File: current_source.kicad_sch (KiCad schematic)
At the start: 7 parts, among them J4 From_E-stop, Q3 S8050, Q4 BSS84, U3 LM317L

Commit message: Termianl block 3d view
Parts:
- J4: value From_E-stop -> TB0010-500-02GR; footprint TerminalBlock:TerminalBlock_MaiXu_MX126-5.0-02P_1x02_P5.00mm -> lighthouse:TerminalBlock_TB0010-500-02GR_1x02_P5.00mm
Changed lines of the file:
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@@
 			)
 		)
-		(property "Value" "From_E-stop"
+		(property "Value" "TB0010-500-02GR"
 			(at 167.64 62.23 0)
 			(effects
@@
 			)
 		)
-		(property "Footprint" "TerminalBlock:TerminalBlock_MaiXu_MX126-5.0-02P_1x02_P5.00mm"
+		(property "Footprint" "lighthouse:TerminalBlock_TB0010-500-02GR_1x02_P5.00mm"
 			(at 167.64 66.04 0)
 			(effects

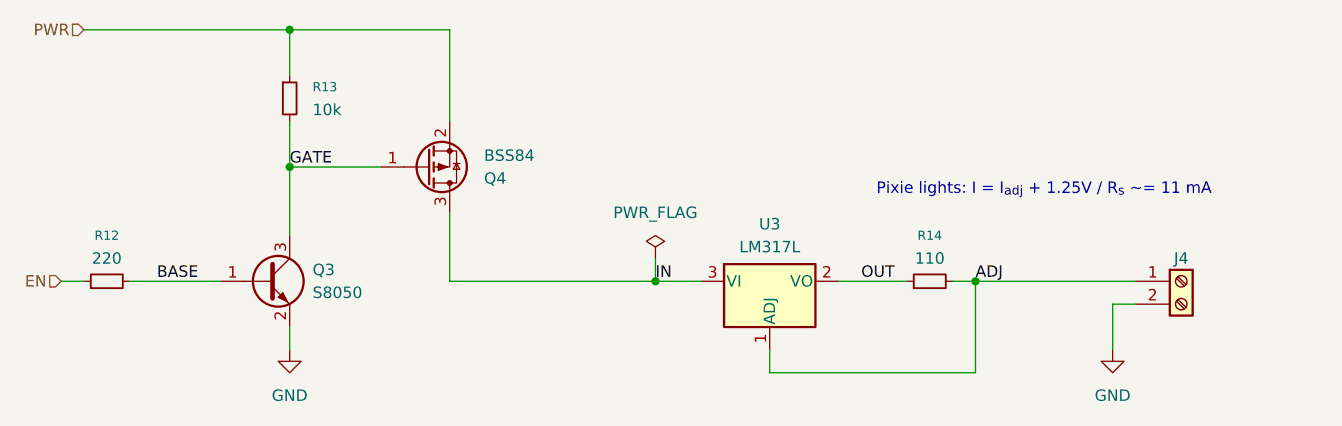
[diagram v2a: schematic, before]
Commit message: Add component attributes
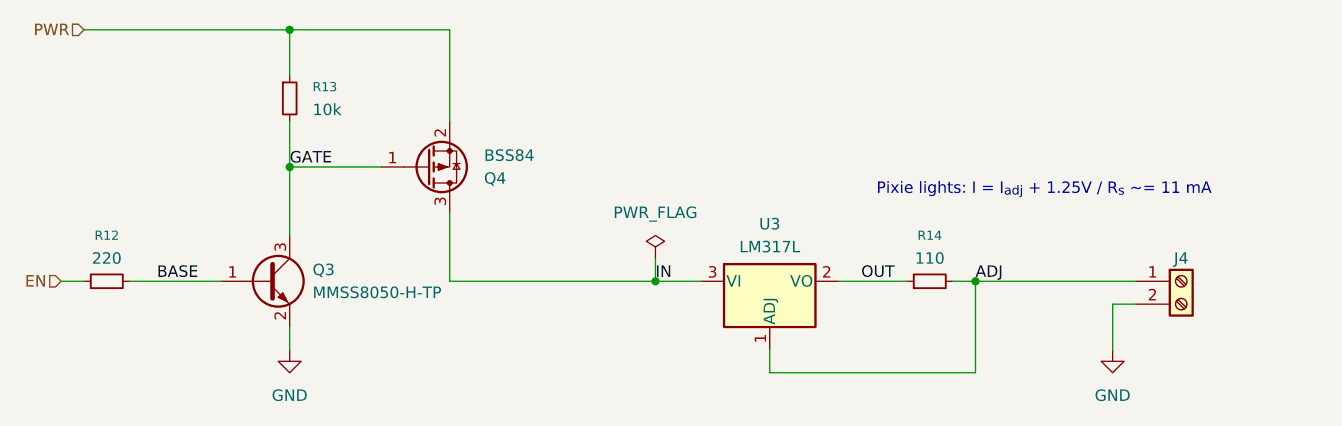
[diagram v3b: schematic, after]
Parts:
- Q3: value S8050 -> MMSS8050-H-TP
- R12: MPN (none) -> CRCW0805220RJNEA; Manufacturer (none) -> Vishay; Mouser Part Number (none) -> 71-CRCW0805220RJNEA; Package (none) -> 0805
- R13: MPN (none) -> CRCW080510K0JNEAC; Manufacturer (none) -> Vishay; Mouser Part Number (none) -> 71-CRCW080510K0JNEAC; Package (none) -> 0805; Power (none) -> 125mW; Tolerance (none) -> 5 %
- R14: MPN (none) -> CRCW0805110RFKEA; Manufacturer (none) -> Vishay; Mouser Part Number (none) -> 71-CRCW0805-110-E3; Package (none) -> 0805; Power (none) -> 250 mW; Tolerance (none) -> 1%
- U3: MPN (none) -> LM317LCPK; Manufacturer (none) -> Texas Instruments; Mouser Part Number (none) -> 595-LM317LCPK
